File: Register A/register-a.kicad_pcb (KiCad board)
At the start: 2 copper layers, 78.7 x 58.4 mm, 50 parts, among them J1 Bus, J2 Address, J3 Misc, J4 Power, U1 74LS245, U2 74LS173, U3 74LS173

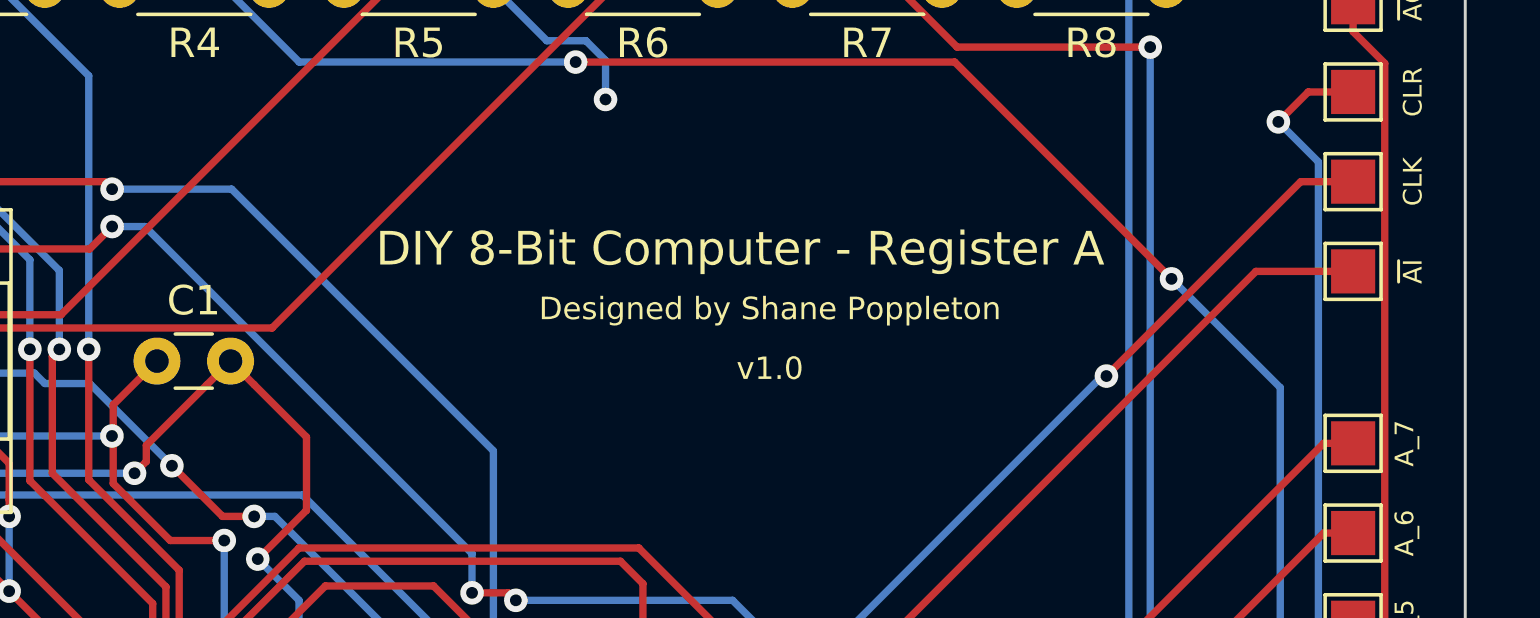
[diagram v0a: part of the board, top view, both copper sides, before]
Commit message: Added Attribution on each PCB, and regenerated gerbers
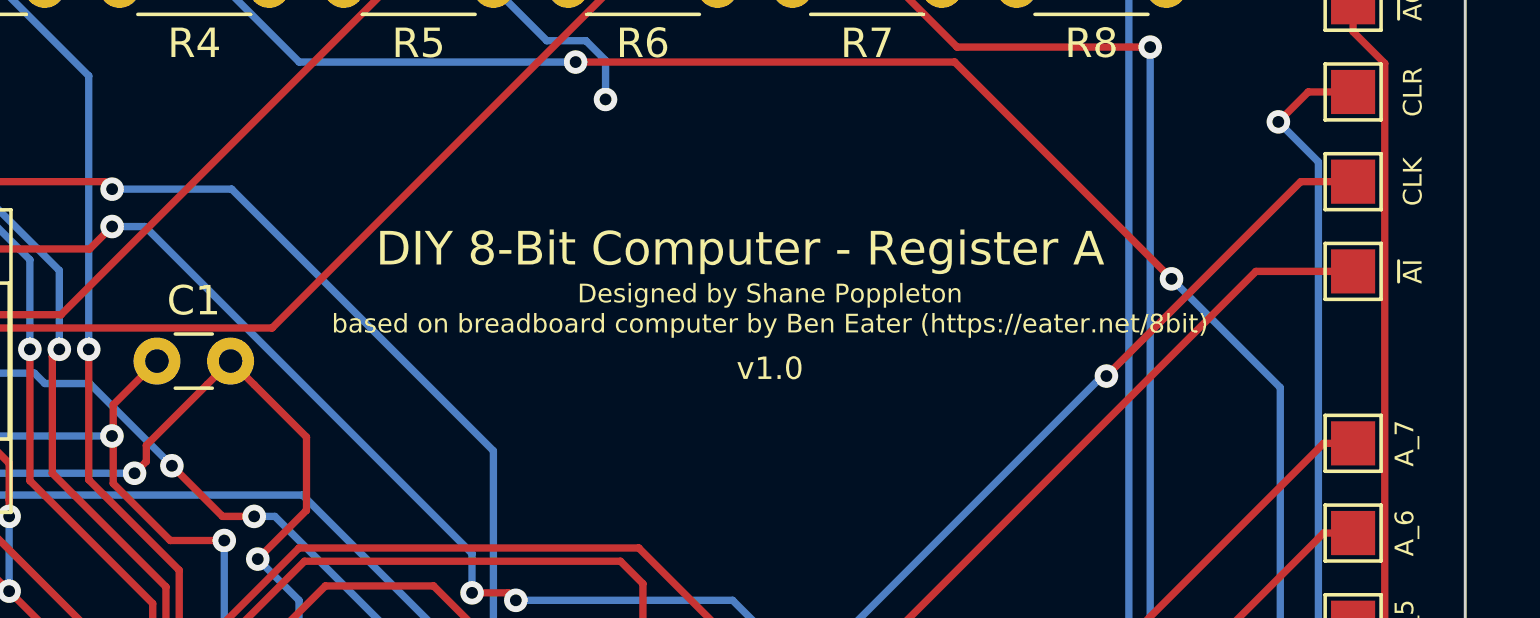
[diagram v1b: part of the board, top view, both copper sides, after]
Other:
- board text added: "Designed by Shane Poppleton based on breadboard computer by Ben Eater (https://eater.net/8bit)"
- board text removed: "Designed by Shane Poppleton"
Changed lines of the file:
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@@
     (effects (font (size 0.762 0.762) (thickness 0.127)))
   )
-  (gr_text "Designed by Shane Poppleton" (at 70.358 49.022) (layer F.SilkS)
-    (effects (font (size 0.762 0.762) (thickness 0.127)))
+  (gr_text "Designed by Shane Poppleton\nbased on breadboard computer by Ben Eater (https://eater.net/8bit)\n" (at 70.358 49.022) (layer F.SilkS)
+    (effects (font (size 0.635 0.635) (thickness 0.1016)))
   )
   (gr_text "DIY 8-Bit Computer - Register A" (at 69.342 46.99) (layer F.SilkS)
